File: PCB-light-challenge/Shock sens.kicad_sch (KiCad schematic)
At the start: 1 part

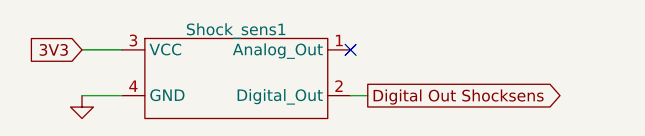
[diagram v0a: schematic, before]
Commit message: main board aangepast en ground toegevoegd
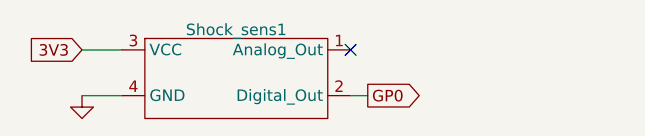
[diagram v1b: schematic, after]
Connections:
- net Digital Out Shocksens renamed GP0
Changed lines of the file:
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@@
     (stroke (width 0) (type default))
   )
-  (global_label "Digital Out Shocksens" (shape output) (at 112.395 71.12 0) (fields_autoplaced)
+  (global_label "GP0" (shape output) (at 112.395 71.12 0) (fields_autoplaced)
     (effects (font (size 1.27 1.27)) (justify left))
-    (property "Intersheetrefs" "${INTERSHEET_REFS}" (at 136.1165 71.12 0)
+    (property "Intersheetrefs" "${INTERSHEET_REFS}" (at 119.0503 71.12 0)
       (effects (font (size 1.27 1.27)) (justify left) hide)
     )

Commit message: PCB 80% af
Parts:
- Shock_sens1: footprint Shocksens:Schock-sens -> Connector_PinHeader_2.54mm:PinHeader_1x03_P2.54mm_Vertical
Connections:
- net 3V3: now also Shock_sens1.1 (VCC); no longer Shock_sens1.3 (VCC)
- net GND: now also Shock_sens1.2 (GND); no longer Shock_sens1.4 (GND)
- net GP0: now also Shock_sens1.3 (Digital_Out); no longer Shock_sens1.2 (Digital_Out)
- no-connect marks 1 -> 0
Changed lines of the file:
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@@
     (company "HHS Living Labs")
   )
-  (no_connect (at 110.49 66.04))
   (wire (pts (xy 80.645 71.12) (xy 85.09 71.12))
     (stroke (width 0) (type default))
@@
       (effects (font (size 1.27 1.27)))
     )
-    (property "Footprint" "Shocksens:Schock-sens" (at 97.79 63.5 0)
+    (property "Footprint" "Connector_PinHeader_2.54mm:PinHeader_1x03_P2.54mm_Vertical" (at 97.79 63.5 0)
       (effects (font (size 1.27 1.27)) hide)
     )
@@
     (pin "2")
     (pin "3")
-    (pin "4")
     (instances
       (project "PCB-light-challenge"
